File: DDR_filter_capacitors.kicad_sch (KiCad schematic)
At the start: 22 parts

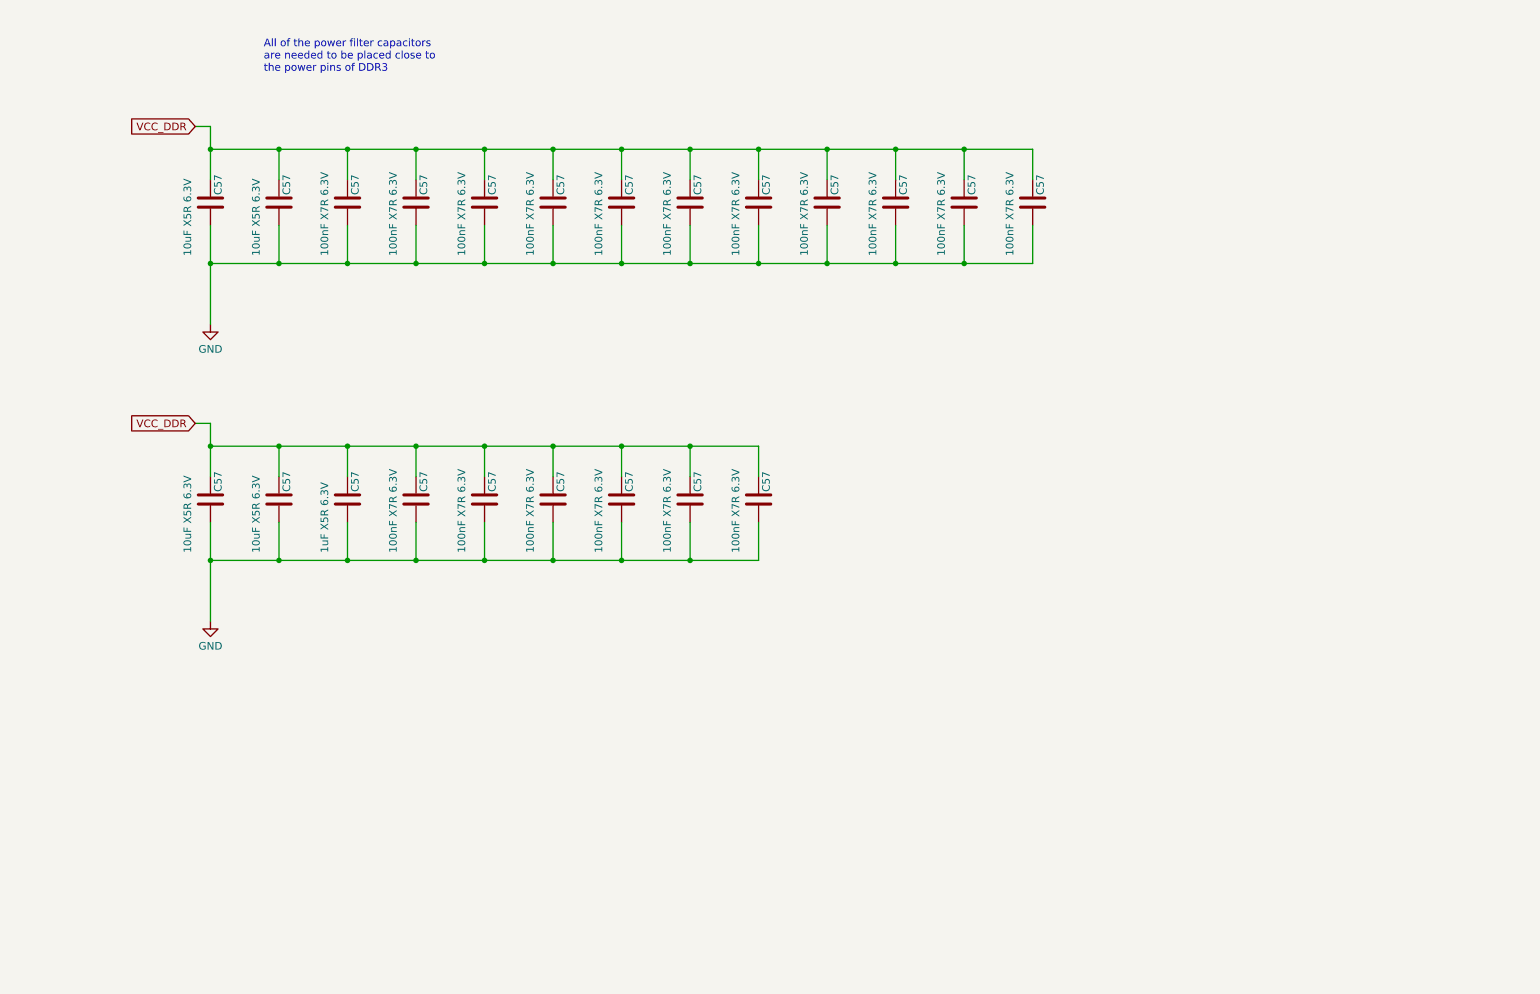
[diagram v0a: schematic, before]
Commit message: replace DDR3 with DDR4
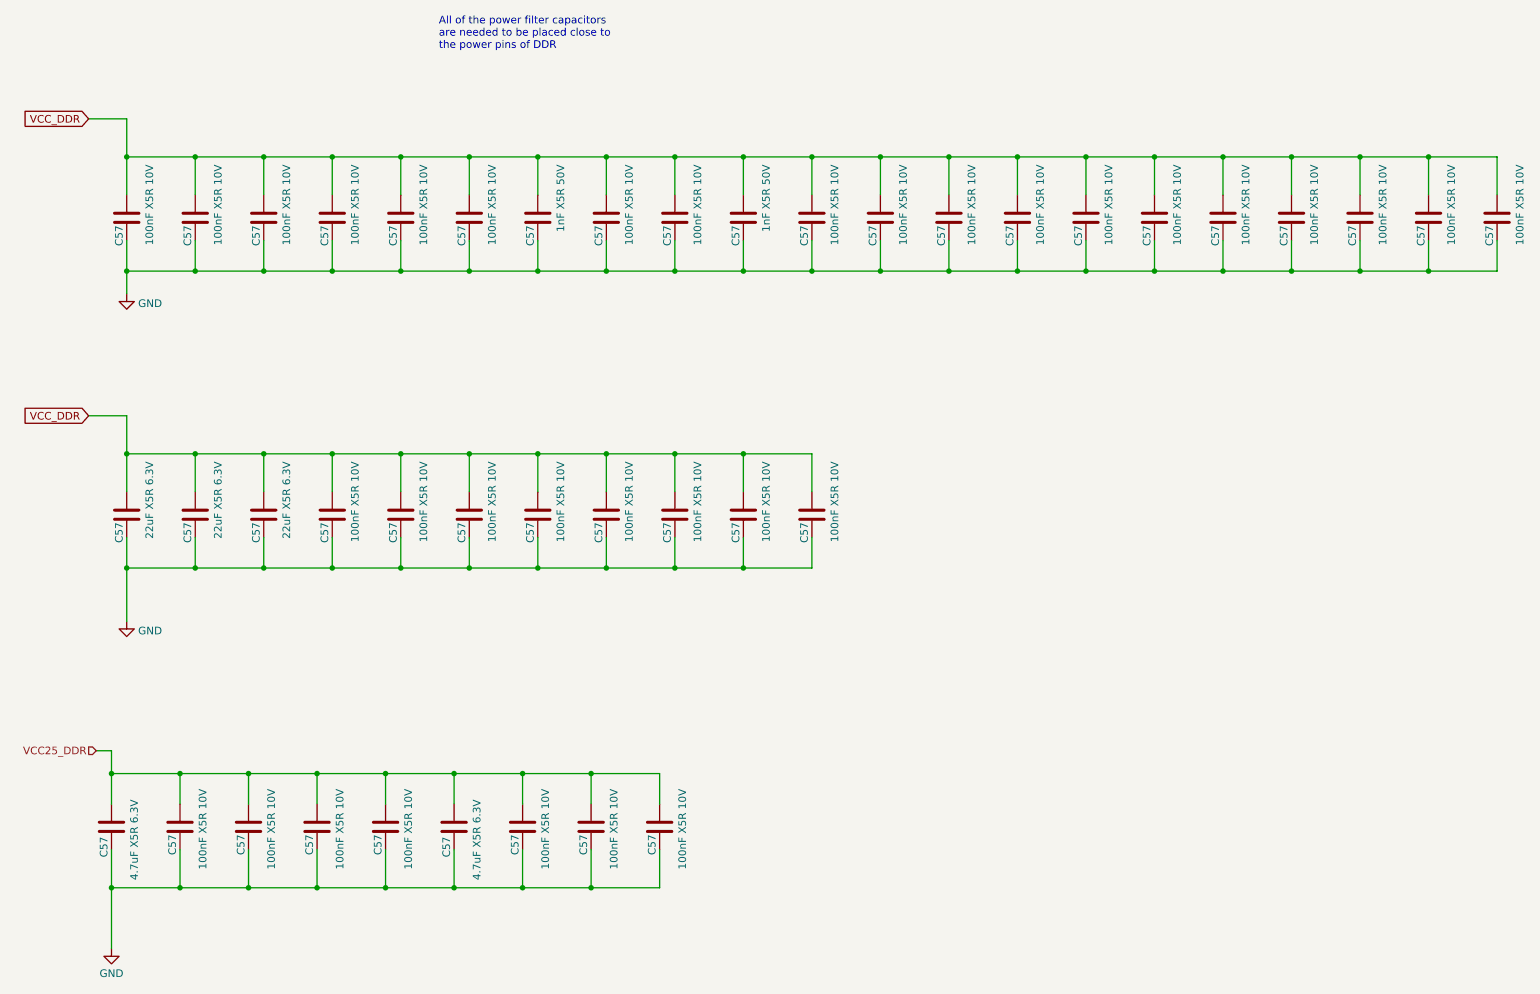
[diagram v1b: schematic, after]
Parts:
- removed C57 (x15): 100nF X7R 6.3V, Capacitor_SMD:C_0402_1005Metric, symbol Device:C
- removed C57 (x3): 10uF X5R 6.3V, Capacitor_SMD:C_0603_1608Metric, symbol Device:C
- removed C57: 1uF X5R 6.3V, Capacitor_SMD:C_0402_1005Metric, symbol Device:C
- added C57 (x33): 100nF X5R 10V, Capacitor_SMD:C_0402_1005Metric, symbol Device:C
- added C57 (x2): 1nF X5R 50V, Capacitor_SMD:C_0402_1005Metric, symbol Device:C
- added C57 (x2): 22uF X5R 6.3V, Capacitor_SMD:C_0603_1608Metric, symbol Device:C
- added C57: 4.7uF X5R 6.3V, Capacitor_SMD:C_0402_1005Metric, symbol Device:C
- C57: value 100nF X7R 6.3V -> 100nF X5R 10V
- C57: value 100nF X7R 6.3V -> 22uF X5R 6.3V; footprint Capacitor_SMD:C_0402_1005Metric -> Capacitor_SMD:C_0603_1608Metric
- C57: value 10uF X5R 6.3V -> 4.7uF X5R 6.3V; footprint Capacitor_SMD:C_0603_1608Metric -> Capacitor_SMD:C_0402_1005Metric
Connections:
- net GND: now also C57.1, C57.1, C57.1, C57.1, C57.1, C57.1, C57.1, C57.1, C57.1, C57.1, C57.1, C57.1, C57.1, C57.1, C57.1, C57.1, C57.1, C57.1, C57.1, C57.1, C57.1, C57.1, C57.1, C57.1, C57.1, C57.1, C57.1, C57.1, C57.1, C57.1, C57.1, C57.1, C57.1, C57.1, C57.1, C57.1, C57.1, C57.1, C57.1, C57.2; no longer C57.2, C57.2
- net VCC_DDR: now also C57.2, C57.2, C57.2, C57.2, C57.2, C57.2, C57.2, C57.2, C57.2, C57.2, C57.2, C57.2, C57.2, C57.2, C57.2, C57.2, C57.2, C57.2, C57.2, C57.2, C57.2, C57.2, C57.2, C57.2, C57.2, C57.2, C57.2, C57.2, C57.2, C57.2, C57.2, C57.2; no longer C57.1, C57.1, C57.1
- new net VCC25_DDR: C57.1, C57.1, C57.2, C57.2, C57.2, C57.2, C57.2, C57.2, C57.2
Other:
- note added: "All of the power filter capacitors are needed to be placed close to the power pins of DDR"
- note removed: "All of the power filter capacitors are needed to be placed close to the power pins of DDR3"
- moved on the sheet: C57

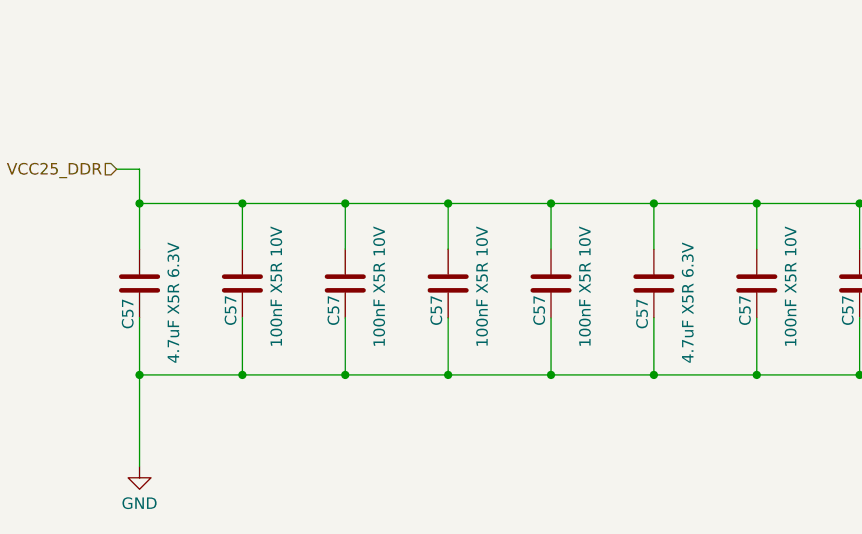
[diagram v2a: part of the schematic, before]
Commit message: updated Capacitors
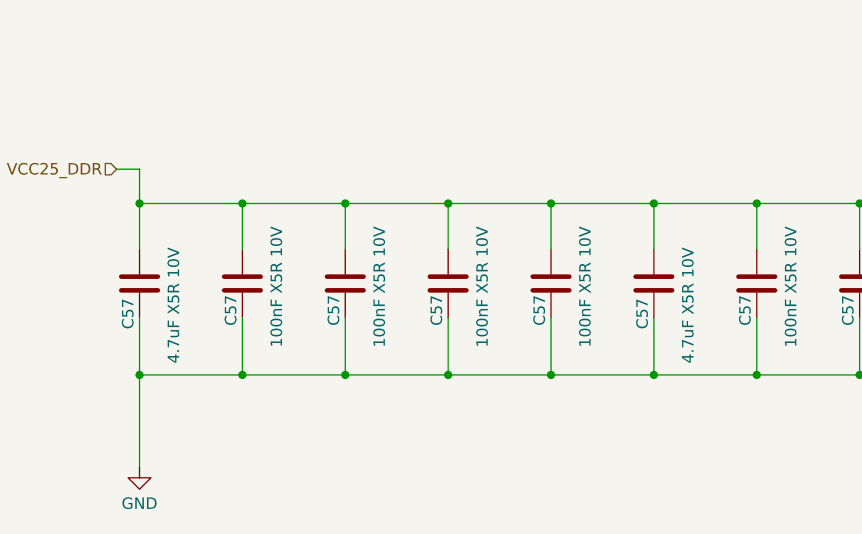
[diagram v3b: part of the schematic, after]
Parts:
- C57: footprint Capacitor_SMD:C_0402_1005Metric -> Capacitor_SMD:C_0201_0603Metric; LCSC (none) -> C76934; Model (none) -> GRM033R61A104KE15D; Vendor (none) -> muRata(村田)
- C57: value 4.7uF X5R 6.3V -> 4.7uF X5R 10V; LCSC (none) -> C77004; Model (none) -> GRM155R61A475KEAAD; Vendor (none) -> muRata(村田)

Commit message: updated LCSC selection of capacitors
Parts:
- C57: LCSC (none) -> C77018; Model (none) -> GRM155R71H102KA01D
- C57: LCSC (none) -> C162690; Model (none) -> ZRB18AR61A226ME01L; Vendor (none) -> muRata(村田)
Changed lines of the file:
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@@
+      (effects (font (size 1.27 1.27)) hide)
+    )
+    (property "Description" "容值: 1nF 精度: ±10% 额定电压: 50V 材质(温度系数): X7R 材质:X7R" (at 142.24 54.61 0)
+      (effects (font (size 1.27 1.27)) hide)
+    )
+    (property "LCSC" "C77018" (at 142.24 54.61 0)
+      (effects (font (size 1.27 1.27)) hide)
+    )
+    (property "Model" "GRM155R71H102KA01D" (at 142.24 54.61 0)
       (effects (font (size 1.27 1.27)) hide)
     )
@@
     )
     (property "Datasheet" "~" (at 107.95 54.61 0)
+      (effects (font (size 1.27 1.27)) hide)
+    )
+    (property "Description" "容值: 1nF 精度: ±10% 额定电压: 50V 材质(温度系数): X7R 材质:X7R" (at 107.95 54.61 0)
+      (effects (font (size 1.27 1.27)) hide)
+    )
+    (property "LCSC" "C77018" (at 107.95 54.61 0)
+      (effects (font (size 1.27 1.27)) hide)
+    )
+    (property "Model" "GRM155R71H102KA01D" (at 107.95 54.61 0)
       (effects (font (size 1.27 1.27)) hide)
     )
@@
       (effects (font (size 1.27 1.27)) hide)
     )
+    (property "Description" "容值: 22uF 精度: ±20% 额定电压: 10V 材质(温度系数): X5R 材质：X5R" (at 62.23 104.14 0)
+      (effects (font (size 1.27 1.27)) hide)
+    )
+    (property "LCSC" "C162690" (at 62.23 104.14 0)
+      (effects (font (size 1.27 1.27)) hide)
+    )
+    (property "Model" "ZRB18AR61A226ME01L" (at 62.23 104.14 0)
+      (effects (font (size 1.27 1.27)) hide)
+    )
+    (property "Vendor" "muRata(村田)" (at 62.23 104.14 0)
+      (effects (font (size 1.27 1.27)) hide)
+    )
     (pin "1")
     (pin "2")
@@
     )
     (property "Datasheet" "~" (at 39.37 104.14 0)
+      (effects (font (size 1.27 1.27)) hide)
+    )
+    (property "Description" "容值: 22uF 精度: ±20% 额定电压: 10V 材质(温度系数): X5R 材质：X5R" (at 39.37 104.14 0)
+      (effects (font (size 1.27 1.27)) hide)
+    )
+    (property "LCSC" "C162690" (at 39.37 104.14 0)
+      (effects (font (size 1.27 1.27)) hide)
+    )
+    (property "Model" "ZRB18AR61A226ME01L" (at 39.37 104.14 0)
+      (effects (font (size 1.27 1.27)) hide)
+    )
+    (property "Vendor" "muRata(村田)" (at 39.37 104.14 0)
       (effects (font (size 1.27 1.27)) hide)
     )
@@
       (effects (font (size 1.27 1.27)) hide)
     )
+    (property "Description" "容值: 22uF 精度: ±20% 额定电压: 10V 材质(温度系数): X5R 材质：X5R" (at 50.8 104.14 0)
+      (effects (font (size 1.27 1.27)) hide)
+    )
+    (property "LCSC" "C162690" (at 50.8 104.14 0)
+      (effects (font (size 1.27 1.27)) hide)
+    )
+    (property "Model" "ZRB18AR61A226ME01L" (at 50.8 104.14 0)
+      (effects (font (size 1.27 1.27)) hide)
+    )
+    (property "Vendor" "muRata(村田)" (at 50.8 104.14 0)
+      (effects (font (size 1.27 1.27)) hide)
+    )

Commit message: layout SoC Power and DDR capacitors
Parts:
- removed C57 (x13): 100nF X5R 10V, Capacitor_SMD:C_0201_0603Metric, symbol Device:C
- removed C57: 1nF X5R 50V, Capacitor_SMD:C_0402_1005Metric, symbol Device:C
- removed C57 (x2): 22uF X5R 6.3V, Capacitor_SMD:C_0603_1608Metric, symbol Device:C
- C57: value 100nF X5R 10V -> 100nF X5R 6.3V; LCSC C76934 -> C76928; Model GRM033R61A104KE15D -> GRM033R60J104KE19D
- C57: footprint Capacitor_SMD:C_0201_0603Metric -> Capacitor_SMD:C_0402_1005Metric
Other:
- moved on the sheet: C57

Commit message: fix some ERCs
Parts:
- renumbered C57 to C?
